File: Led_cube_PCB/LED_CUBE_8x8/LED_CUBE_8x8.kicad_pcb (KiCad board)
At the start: 2 copper layers, 100 x 100 mm, 318 parts, among them IC1 74AHCT244PW,118, IC10 74AHCT244PW,118, IC11 74AHCT244PW,118, IC12 74AHCT244PW,118, IC13 74AHCT244PW,118, IC14 74AHCT244PW,118, IC15 74AHCT244PW,118, IC16 74AHCT244PW,118, IC17 74AHCT244PW,118, IC18 74AHCT244PW,118, IC19 74AHCT244PW,118, IC2 74AHCT244PW,118, IC20 74AHCT244PW,118, IC21 74AHCT244PW,118, IC22 74AHCT244PW,118, IC23 74AHCT244PW,118, IC24 74AHCT244PW,118, IC25 74AHCT244PW,118, IC26 SN74HCS238DYYR, IC27 SN74HCS238DYYR, IC29 STM32C071C8T6, IC3 74AHCT244PW,118, IC30 TPS62A01DRLR, IC31 SN74HCS238DYYR, IC32 TBD62083AFNG,EL, IC4 74AHCT244PW,118, IC5 74AHCT244PW,118, IC6 74AHCT244PW,118, IC7 SN74HCS238DYYR, IC8 74AHCT244PW,118, IC9 74AHCT244PW,118, J10 1984963, J2 20021121-00014T4LF, J3 Conn_02x16_Odd_Even, J4 Conn_02x16_Odd_Even, J5 Conn_02x16_Odd_Even, J6 Conn_02x16_Odd_Even, J7 Conn_02x16_Odd_Even, J8 Conn_02x16_Odd_Even, J9 Conn_02x04_Top_Bottom, Y1 CX3225FB48000F0FZZH1

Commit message: Top layer placement done revised the SWD connector and started routing.
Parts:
- removed C44: C10uF, Capacitor_SMD:C_0603_1608Metric_Pad1.08x0.95mm_HandSolder
- removed J2: 20021121-00014T4LF, SamacSys_Parts:2002112100014T4LF
- removed R14, R15, R16, R30, R32, R33, R34, R35, R41, R42, R43, R44, R48, R49, R50, R51, R58: R10K, Resistor_SMD:R_0603_1608Metric_Pad0.98x0.95mm_HandSolder
- added J1: FTSH-107-01-L-DV-K-A, SamacSys_Parts:FTSH-107-XX-YYY-DV-K-A, F.Cu at (178.0, 117.9)
- added R250: R10K, Resistor_SMD:R_0603_1608Metric_Pad0.98x0.95mm_HandSolder, F.Cu at (157.5, 128.7)
- added REF**: MountingHole_3.2mm_M3, MountingHole:MountingHole_3.2mm_M3, F.Cu at (196.4, 142.9)
- added REF**: MountingHole_3.2mm_M3, MountingHole:MountingHole_3.2mm_M3, F.Cu at (196.4, 51.6)
- added REF**: MountingHole_3.2mm_M3, MountingHole:MountingHole_3.2mm_M3, F.Cu at (105.1, 142.9)
- added REF**: MountingHole_3.2mm_M3, MountingHole:MountingHole_3.2mm_M3, F.Cu at (105.1, 51.6)
- C1, C10, C11, C12, C13, C14, C15, C16, C17, C18, C19, C2, C20, C21, C22, C23, C24, C3, C4, C5, C6, C7, C8, C9, IC1, IC10, IC11, IC12, IC13, IC14, IC15, IC16, IC17, IC18, IC19, IC2, IC20, IC21, IC22, IC23, IC24, IC25, IC26, IC27, IC3, IC4, IC5, IC6, IC7, IC8, IC9, R1, R10, R11, R12, R13, R18, R19, R2, R20, R21, R26, R27, R28, R29, R3, R31, R36, R37, R38, R39, R4, R40, R45, R46, R47, R5, R6: moved to B.Cu
- J3, J4, J5, J6, J7, J8: footprint Connector_PinHeader_1.00mm:PinHeader_2x16_P1.00mm_Vertical -> Connector_PinSocket_2.54mm:PinSocket_2x16_P2.54mm_Vertical
- moved J10 357.5 mm to (183.0, 141.3)
- moved IC29 337.1 mm to (165.5, 119.2)
- moved C41 335.6 mm to (172.3, 114.5), turned to 90 degrees
- moved C33 335.6 mm to (169.7, 139.9), turned to -90 degrees
- moved C32 333.8 mm to (168.6, 131.2), turned to 90 degrees
- moved JP3 331.7 mm to (172.2, 139.9), turned to 90 degrees
- moved C34 331.4 mm to (166.4, 134.8), turned to 90 degrees
- moved D1 329.9 mm to (166.0, 140.0), turned to -90 degrees
- moved R56 328.1 mm to (168.0, 139.9), turned to -90 degrees
- moved IC30 328.0 mm to (168.6, 134.0), turned to 180 degrees
- moved L1 326.2 mm to (172.2, 135.0), turned to 90 degrees
- moved R57 324.2 mm to (164.8, 134.8), turned to 90 degrees
- moved R55 323.0 mm to (163.1, 134.8), turned to -90 degrees
- moved C40 322.8 mm to (159.3, 119.1), turned to -90 degrees
- moved C43 320.9 mm to (157.6, 119.1), turned to -90 degrees
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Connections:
- C24 pad 1: GND -> +5V
- C24 pad 2: +5V -> GND
- IC29 pad 2: unconnected-(IC29-PC14-OSCX_IN-Pad2) -> DB1
- IC29 pad 35: DB1 -> SWDIO
- IC29 pad 36: Net-(IC29-PA14-BOOT0) -> SWCLK
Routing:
- net +3.3V: track 0.00 -> 49.8 mm
- net USART1_TX: track 0.00 -> 47.4 mm, vias 0 -> 2
- net USART1_RX: track 0.00 -> 37.7 mm, vias 0 -> 2
- net LS_0: track 0.00 -> 36.4 mm
- net LS_2: track 0.00 -> 34.5 mm
- net LS_1: track 0.00 -> 33.1 mm
- net +5V: track 0.00 -> 26.5 mm
- net Ena_L8: track 0.00 -> 19.6 mm
- net NRST: track 0.00 -> 16.6 mm
- net O_L1: track 0.00 -> 15.8 mm
- net Ena_L7: track 0.00 -> 15.2 mm
- net O_L6: track 0.00 -> 15.2 mm
- net O_L8: track 0.00 -> 15.2 mm
- net O_L4: track 0.00 -> 15.0 mm
- net O_L2: track 0.00 -> 15.0 mm
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- added copper zone on F.Cu, net FB
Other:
- outline, holes or cut-outs redrawn
- copper layers 2 -> 4

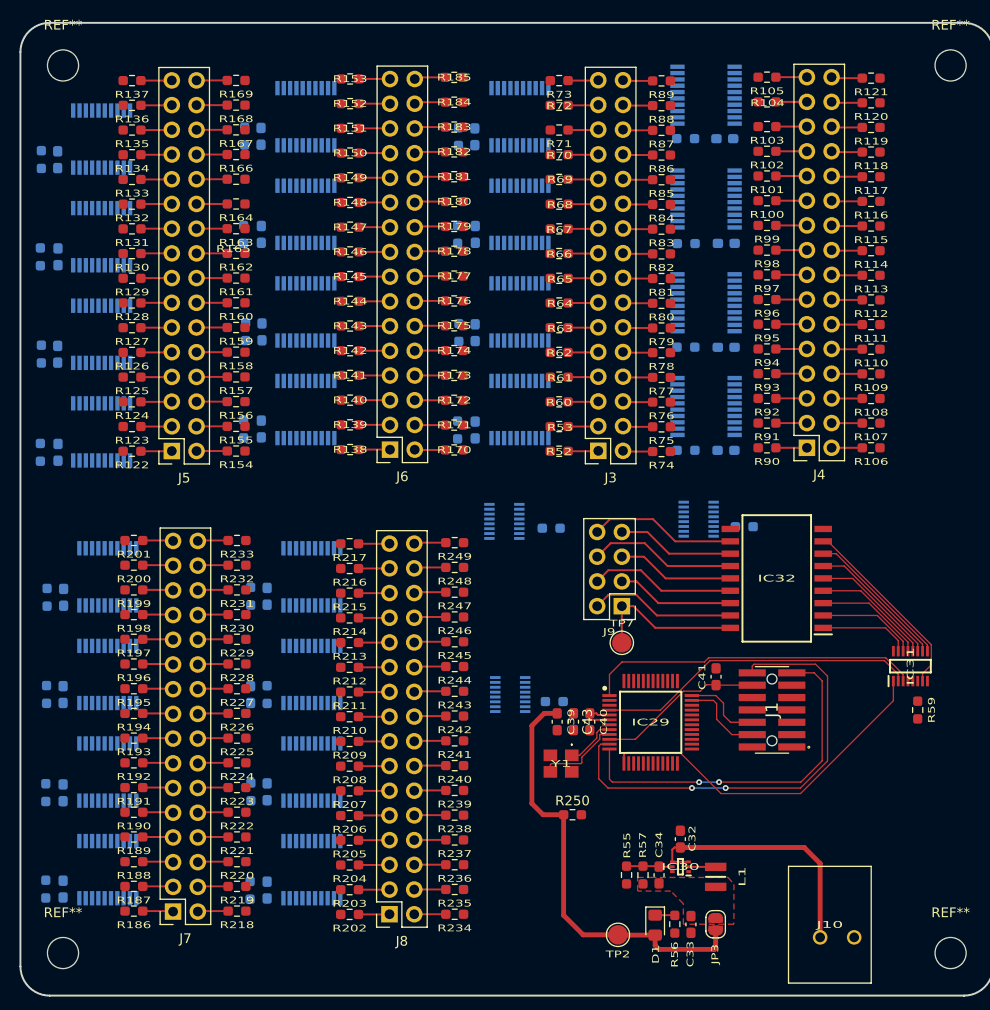
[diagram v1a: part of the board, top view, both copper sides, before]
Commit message: Progressed with routing traces back of PCB.
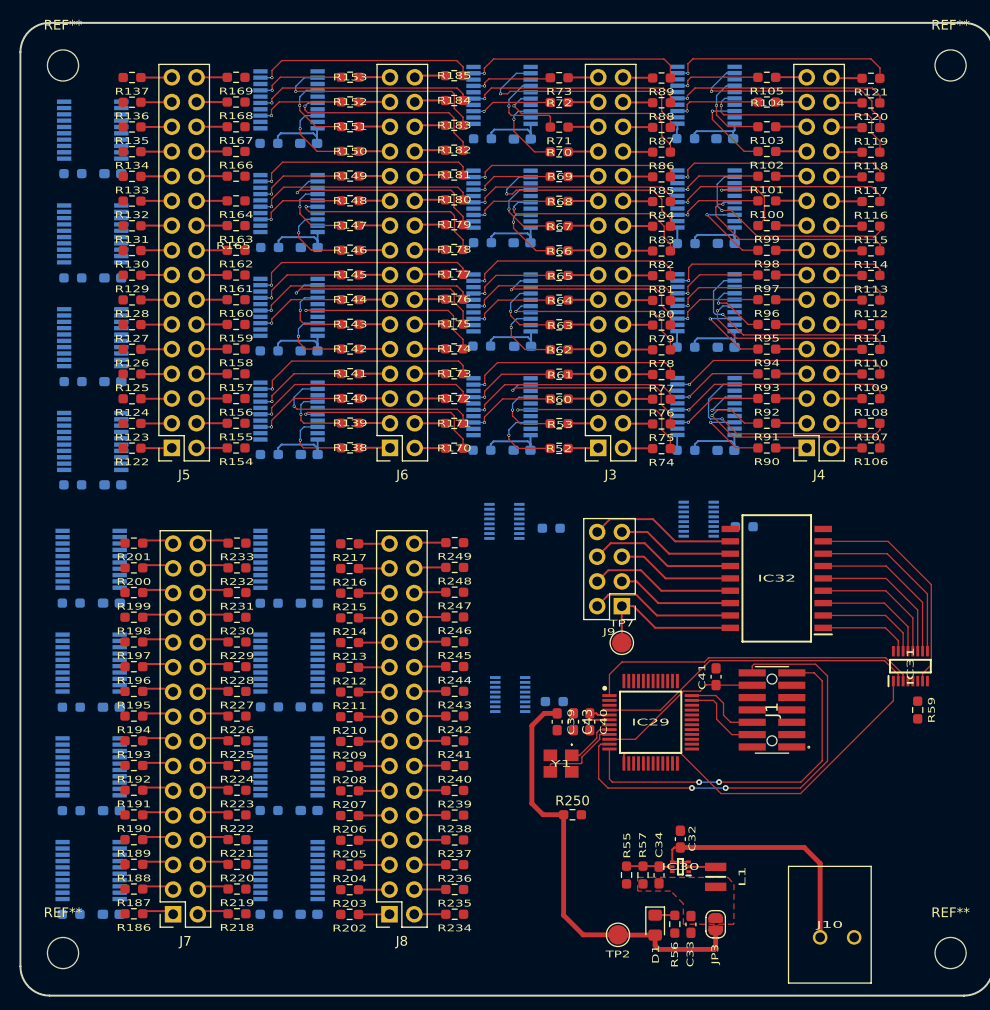
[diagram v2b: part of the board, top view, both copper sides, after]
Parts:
- moved C1 6.56 mm to (110.3, 94.7), turned to 0 degrees
- moved C10 6.33 mm to (110.2, 84.1), turned to 0 degrees
- moved C20 6.15 mm to (130.4, 117.6), turned to 0 degrees
- moved C2 6.04 mm to (110.2, 73.5), turned to 0 degrees
- moved C11 5.85 mm to (110.2, 62.8), turned to 0 degrees
- moved C12 5.59 mm to (110.1, 138.9), turned to 0 degrees
- moved C3 5.58 mm to (130.4, 91.6), turned to 0 degrees
- moved C23 5.30 mm to (110.1, 128.2), turned to 0 degrees
- moved C5 5.25 mm to (152.3, 91.2), turned to 0 degrees
- moved C8 5.23 mm to (130.4, 81.0), turned to 0 degrees
- moved C14 5.13 mm to (110.1, 117.6), turned to 0 degrees
- moved C7 5.11 mm to (130.4, 70.3), turned to 0 degrees
- moved C18 5.08 mm to (152.4, 80.5), turned to 0 degrees
- moved C15 4.98 mm to (130.4, 138.9), turned to 0 degrees
- moved C24 4.96 mm to (110.1, 106.9), turned to 180 degrees
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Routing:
- net +5V: track 26.5 -> 112.1 mm
- net R_COL28: track 0.00 -> 24.7 mm, vias 0 -> 1
- net R_COL36: track 0.00 -> 24.3 mm, vias 0 -> 1
- net R_COL44: track 0.00 -> 23.7 mm, vias 0 -> 1
- net G_COL40: track 0.00 -> 23.6 mm, vias 0 -> 1
- net G_COL38: track 0.00 -> 23.5 mm, vias 0 -> 1
- net R_COL64: track 0.00 -> 23.4 mm, vias 0 -> 1
- net G_COL48: track 0.00 -> 23.4 mm, vias 0 -> 1
- net R_COL60: track 0.00 -> 23.4 mm, vias 0 -> 1
- net G_COL56: track 0.00 -> 23.2 mm, vias 0 -> 1
- net G_COL46: track 0.00 -> 23.2 mm, vias 0 -> 1
- net G_COL64: track 0.00 -> 23.2 mm, vias 0 -> 1
- net G_COL60: track 0.00 -> 23.2 mm, vias 0 -> 1
- net R_COL48: track 0.00 -> 23.1 mm, vias 0 -> 1
- net R_COL52: track 0.00 -> 23.1 mm, vias 0 -> 1
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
